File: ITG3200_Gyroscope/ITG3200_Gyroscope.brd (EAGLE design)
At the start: 39.7 x 26.7 mm, 5 parts

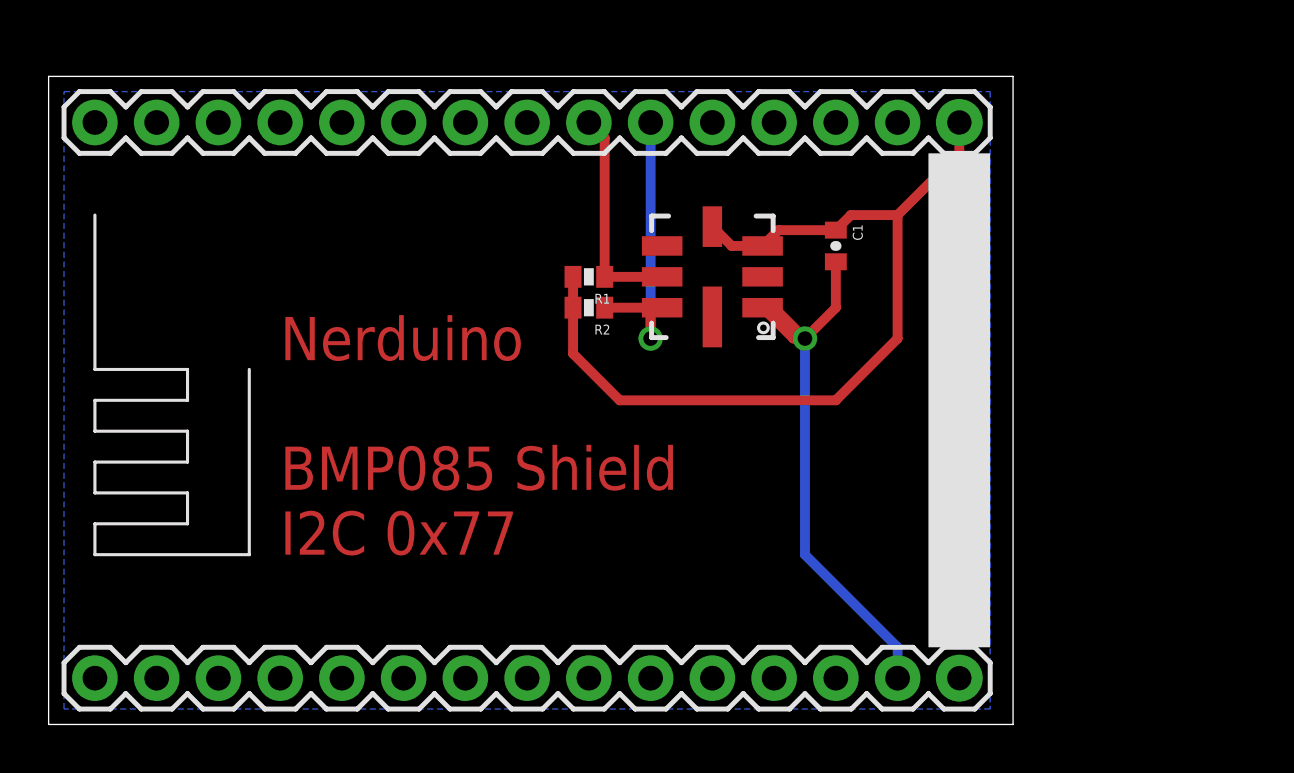
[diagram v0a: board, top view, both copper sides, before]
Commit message: Updated stencil text Added PCA9685 and ITG3200 shields
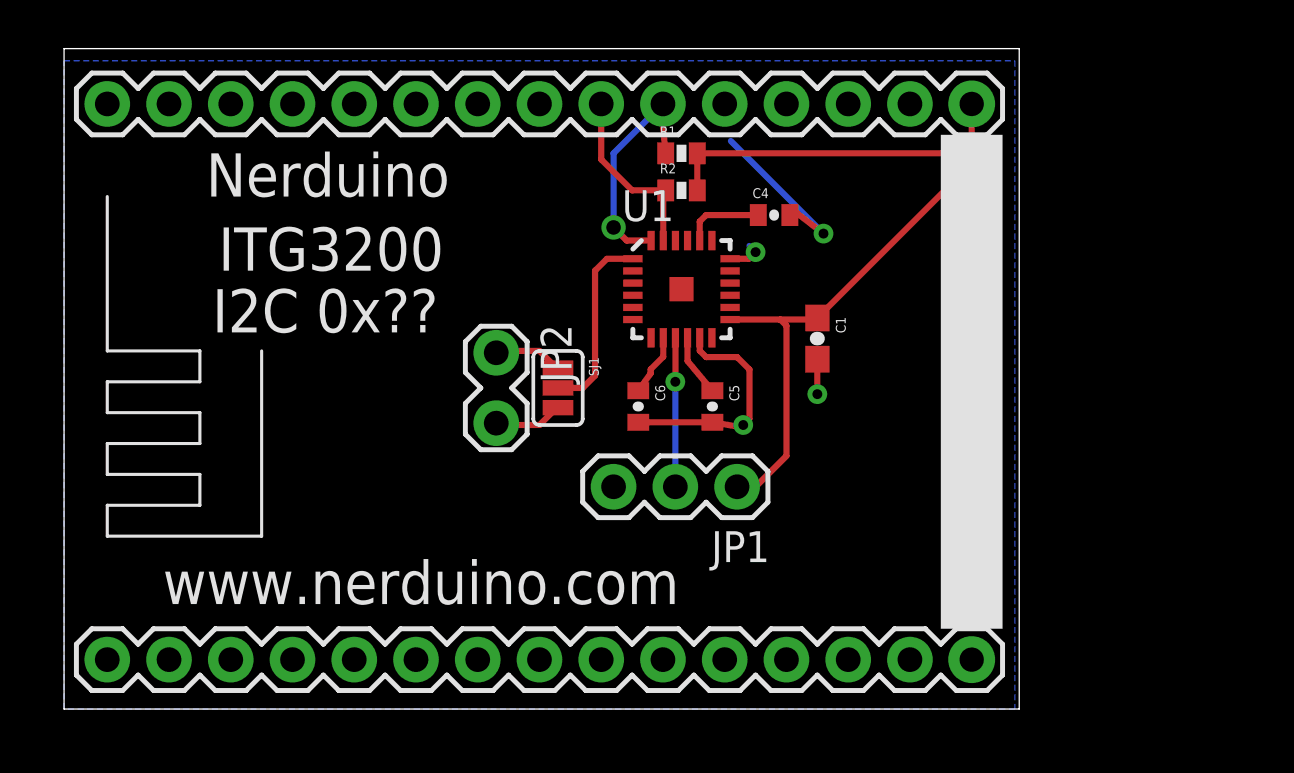
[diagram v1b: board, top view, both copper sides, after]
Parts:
- removed U$1: NERDSHIELD, NerduinoShieldLib:NERDUINO_STACK
- added C4: 2.2nF, SparkFun:0402-CAP
- added C5: .1uF, SparkFun:0402-CAP
- added C6: 10nF, SparkFun:0402-CAP
- added JP1: JP1, SparkFun:1X03
- added JP2: (no value), SparkFun:1X02_LOCK
- added SJ1: ClockSource, SparkFun:SJ_3_PASTE2&3
- added U1: ITG-3200, SparkFun:QFN-24
- C1: value 0.1uF -> .1uF; device SparkFun:0402-CAP -> SparkFun:0603-CAP
- R1, R2: value 4.7k -> 4.7K
- U$2: value BMP085 -> NERDSHIELD; device SparkFun:BMP085 -> NerduinoShieldLib:NERDUINO_STACK
- moved U$2 12.8 mm to (19.6, 7.11), turned to 0 degrees
- moved R1 6.35 mm to (25.4, 22.9), turned to 0 degrees
- moved R2 6.15 mm to (25.4, 21.3), turned to 0 degrees
- moved C1 3.89 mm to (31.0, 15.2)
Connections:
- removed net 3.3V: C1.1, R1.2, R2.2, U$1.16, U$2.3, U$2.4
- removed net N$3: R1.1, U$1.22, U$2.6
- new net +3V3: C1.1, JP1.1, R1.2, R2.2, U$2.16, U1.13
- new net N$1: JP1.2, U1.9
- new net N$10: JP2.1, SJ1.1
- new net N$11: SJ1.2, U1.1
- new net N$5: R2.1, U$2.22, U1.23
- new net N$6: C4.1, U1.20
- new net N$7: C5.1, U1.10
- new net N$8: C6.1, U1.8
- net GND: now also C4.2, C5.2, C6.2, JP1.3, JP2.2, SJ1.3, U$2.10, U$2.14, U$2.17, U$2.24, U1.11, U1.18; no longer U$1.14, U$2.1
- net N$2: now also R1.1, U$2.21, U1.24; no longer R2.1, U$1.21, U$2.7
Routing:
- net 3.3V: track 36.8 -> 0.00 mm
- net +3V3: track 0.00 -> 36.4 mm
- net N$3: track 8.98 -> 0.00 mm
- net N$11: track 0.00 -> 7.81 mm
- net N$5: track 0.00 -> 7.57 mm
- net N$1: track 0.00 -> 6.13 mm, vias 0 -> 1
- net N$6: track 0.00 -> 3.30 mm
- net N$10: track 0.00 -> 2.87 mm
- net N$2: track 12.5 -> 9.77 mm
- net N$8: track 0.00 -> 2.55 mm
- net N$7: track 0.00 -> 2.55 mm
- net GND: track 23.8 -> 23.1 mm, vias 1 -> 4
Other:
- board size 39.7 x 26.7 mm -> 39.3 x 27.2 mm
- board text added: "I2C 0x??"
- board text added: "ITG3200"
- board text added: "Nerduino"
- board text added: "www.nerduino.com"
- board text removed: "Nerduino BMP085 Shield I2C 0x77"

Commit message: Added OLED Shield Added LiPo Battery Charger Shield Updated outlines of all shields to match the cutout of the nodemcu board
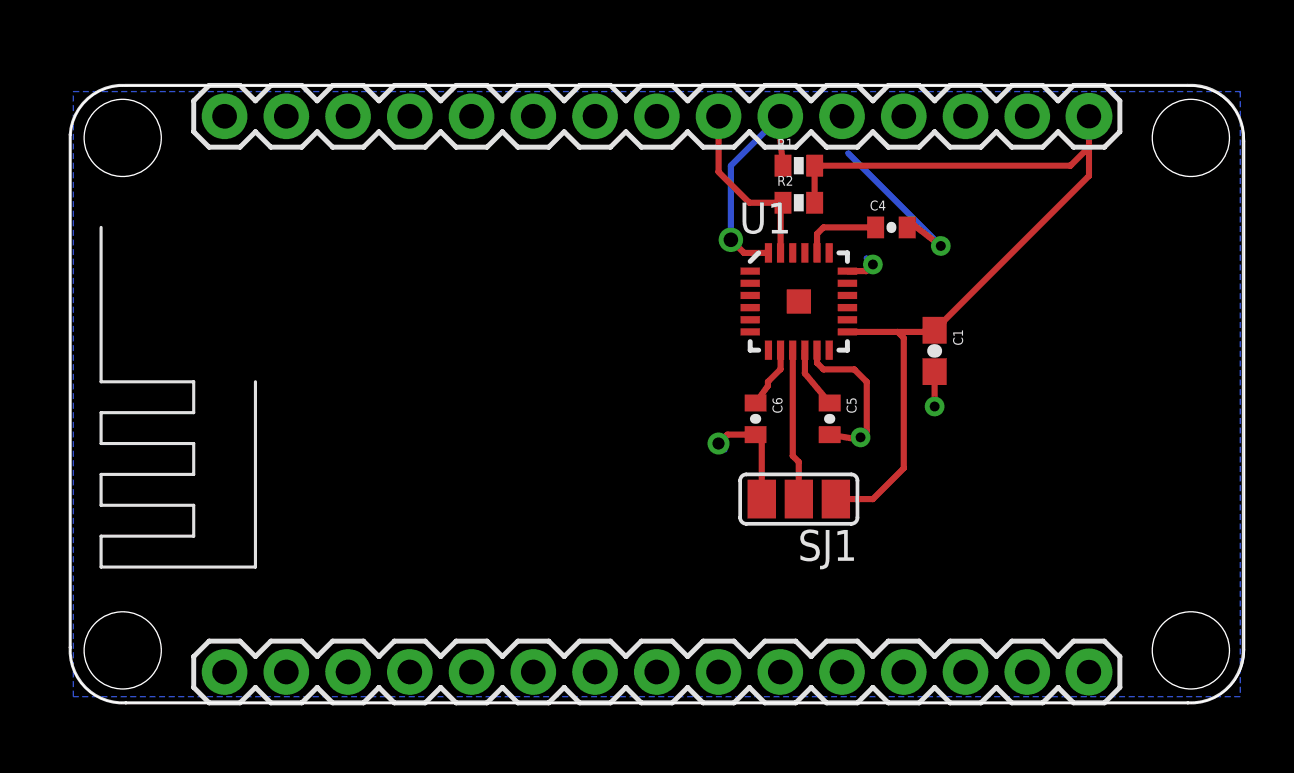
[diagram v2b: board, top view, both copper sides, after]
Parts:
- removed JP1: JP1, SparkFun:1X03
- removed JP2: (no value), SparkFun:1X02_LOCK
- SJ1: value ClockSource -> (none); device SparkFun:SJ_3_PASTE2&3 -> SparkFun:SJ_2
- moved SJ1 10.9 mm to (30.2, 8.64), turned to 180 degrees
- moved C1 4.85 mm to (35.8, 14.7)
- moved C4 4.85 mm to (34.0, 19.8)
- moved C6 4.85 mm to (28.4, 11.9)
- moved R1 4.85 mm to (30.2, 22.4)
- moved R2 4.85 mm to (30.2, 20.8)
- moved U$2 4.85 mm to (24.4, 6.60)
- moved U1 4.85 mm to (30.2, 16.8)
- moved C5 4.85 mm to (31.5, 11.9)
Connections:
- removed net N$10: JP2.1, SJ1.1
- removed net N$11: SJ1.2, U1.1
- net +3V3: now also SJ1.1; no longer JP1.1
- net GND: now also U1.1; no longer JP1.3, JP2.2
- net N$1: now also SJ1.2; no longer JP1.2
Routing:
- net N$11: track 7.81 -> 0.00 mm
- net N$10: track 2.87 -> 0.00 mm
- net GND: track 23.1 -> 21.9 mm, vias 4 -> 5
- net +3V3: track 36.4 -> 37.2 mm
- net N$1: track 6.13 -> 6.23 mm, vias 1 -> 0
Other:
- board size 39.3 x 27.2 mm -> 48.3 x 25.4 mm
- board text added: "NERDUINO ITG3200 Shield I2C 0x?? www.nerduino.com"
- board text removed: "I2C 0x??"
- board text removed: "ITG3200"
- board text removed: "Nerduino"
- board text removed: "www.nerduino.com"

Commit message: Updated the i2c pins to all shields to use d11/d12  as these pins will have dual use with the upcoming wifimcu Added FM24W256  Fram shield Added X95840 Digital potentiometer Shield Added AD5696 DAC Shield
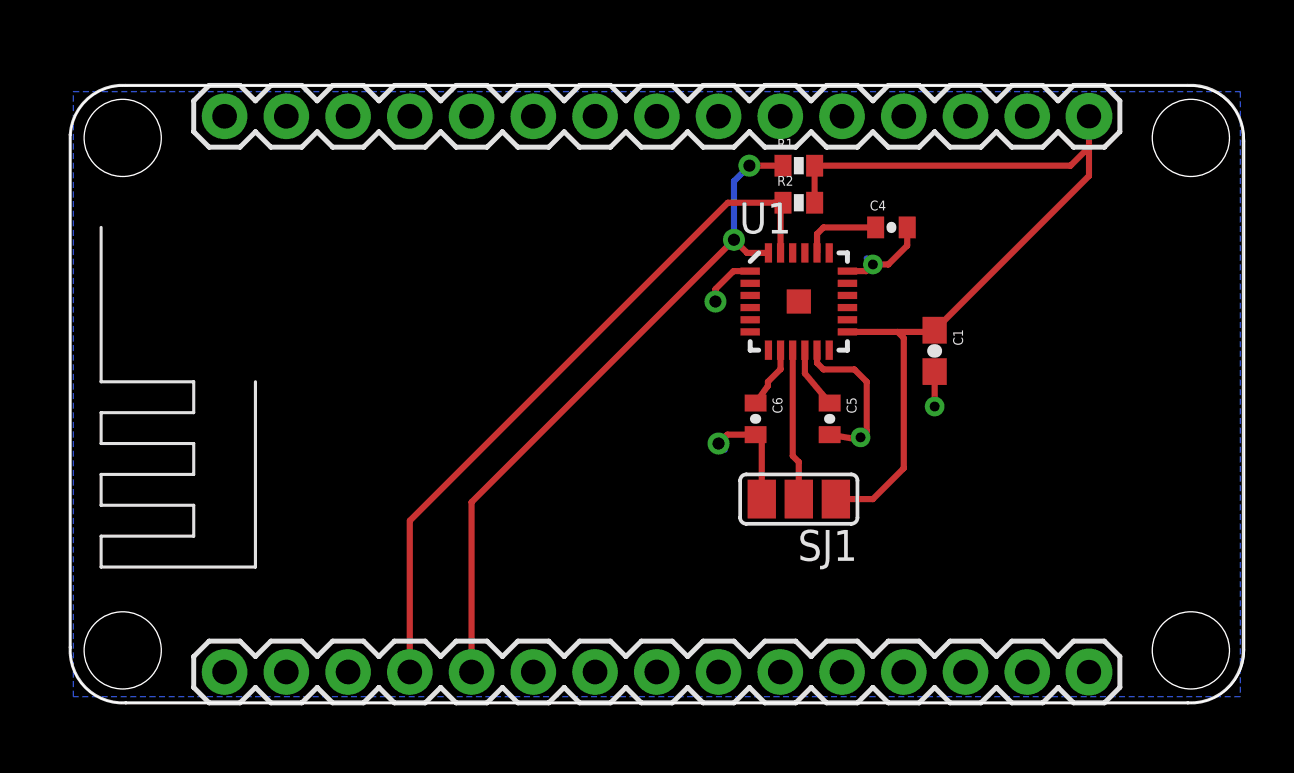
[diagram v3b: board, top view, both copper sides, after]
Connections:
- net GND: no longer U$2.24
- net N$2: now also U$2.5; no longer U$2.21
- net N$5: now also U$2.4; no longer U$2.22
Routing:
- net N$5: track 7.57 -> 29.1 mm
- net N$2: track 9.77 -> 28.6 mm, vias 1 -> 2
- net GND: track 21.9 -> 19.9 mm
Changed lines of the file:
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@@
 <contactref element="C5" pad="2"/>
 <contactref element="C4" pad="2"/>
-<wire x1="34.686" y1="19.812" x2="34.964" y2="19.9" width="0.254" layer="1"/>
-<wire x1="34.964" y1="19.9" x2="36.068" y2="19.05" width="0.254" layer="1"/>
-<wire x1="36.068" y1="19.05" x2="32.258" y2="22.86" width="0.254" layer="16"/>
 <wire x1="32.226" y1="18.014" x2="33" y2="18.014" width="0.254" layer="1"/>
 <wire x1="33" y1="18.014" x2="33.274" y2="18.288" width="0.254" layer="1"/>
@@
 <wire x1="35.814" y1="13.882" x2="35.814" y2="12.446" width="0.254" layer="1"/>
 <wire x1="35.814" y1="12.446" x2="36.068" y2="12.446" width="0.254" layer="16"/>
-<via x="36.068" y="19.05" extent="1-16" drill="0.4064" diameter="0.4064" shape="octagon"/>
 <via x="33.274" y="18.288" extent="1-16" drill="0.4064" diameter="0.4064" shape="octagon"/>
 <via x="32.766" y="11.176" extent="1-16" drill="0.4064" diameter="0.4064" shape="octagon"/>
@@
 </polygon>
 <contactref element="U$2" pad="17"/>
-<contactref element="U$2" pad="24"/>
 <contactref element="U$2" pad="14"/>
 <contactref element="U$2" pad="10"/>
@@
 <via x="26.924" y="10.922" extent="1-16" drill="0.5"/>
 <wire x1="26.924" y1="10.922" x2="27.178" y2="10.668" width="0.254" layer="16"/>
-<wire x1="32.226" y1="18.014" x2="28.226" y2="18.014" width="0" layer="19" extent="1-1"/>
+<wire x1="28.226" y1="18.014" x2="27.539" y2="18.014" width="0.254" layer="1"/>
+<wire x1="27.539" y1="18.014" x2="26.797" y2="17.272" width="0.254" layer="1"/>
+<wire x1="26.797" y1="17.272" x2="26.797" y2="16.764" width="0.254" layer="1"/>
+<via x="26.797" y="16.764" extent="1-16" drill="0.5"/>
+<wire x1="26.797" y1="16.764" x2="26.67" y2="16.764" width="0.254" layer="16"/>
+<wire x1="26.67" y1="16.764" x2="26.543" y2="16.891" width="0.254" layer="16"/>
+<wire x1="34.686" y1="19.812" x2="34.686" y2="19.065" width="0.254" layer="1"/>
+<wire x1="34.686" y1="19.065" x2="33.909" y2="18.288" width="0.254" layer="1"/>
+<wire x1="33.909" y1="18.288" x2="33.274" y2="18.288" width="0.254" layer="1"/>
 </signal>
 <signal name="N$2">
 <contactref element="R1" pad="1"/>
 <contactref element="U1" pad="24"/>
-<contactref element="U$2" pad="21"/>
-<wire x1="28.976" y1="18.764" x2="27.972" y2="18.764" width="0.254" layer="1"/>
-<wire x1="27.972" y1="18.764" x2="27.432" y2="19.304" width="0.254" layer="1"/>
-<via x="27.432" y="19.304" extent="1-16" drill="0.6" shape="square"/>
-<wire x1="27.432" y1="19.304" x2="27.432" y2="22.352" width="0.254" layer="16"/>
-<wire x1="27.432" y1="22.352" x2="29.464" y2="24.384" width="0.254" layer="16"/>
-<wire x1="29.576" y1="22.352" x2="29.376" y2="24.296" width="0.254" layer="1"/>
-<wire x1="29.376" y1="24.296" x2="29.464" y2="24.384" width="0.254" layer="1"/>
+<contactref element="U$2" pad="5"/>
+<wire x1="16.764" y1="1.524" x2="16.764" y2="8.509" width="0.254" layer="1"/>
+<wire x1="16.764" y1="8.509" x2="27.559" y2="19.304" width="0.254" layer="1"/>
+<via x="27.559" y="19.304" extent="1-16" drill="0.5"/>
+<wire x1="27.559" y1="19.304" x2="27.559" y2="21.717" width="0.254" layer="16"/>
+<wire x1="27.559" y1="21.717" x2="28.194" y2="22.352" width="0.254" layer="16"/>
+<via x="28.194" y="22.352" extent="1-16" drill="0.5"/>
+<wire x1="28.194" y1="22.352" x2="29.576" y2="22.352" width="0.254" layer="1"/>
+<wire x1="28.976" y1="18.764" x2="28.099" y2="18.764" width="0.254" layer="1"/>
+<wire x1="28.099" y1="18.764" x2="27.559" y2="19.304" width="0.254" layer="1"/>
 </signal>
 <signal name="N$5">
 <contactref element="R2" pad="1"/>
 <contactref element="U1" pad="23"/>
-<contactref element="U$2" pad="22"/>
-<wire x1="26.924" y1="24.384" x2="26.924" y2="22.098" width="0.254" layer="1"/>
-<wire x1="26.924" y1="22.098" x2="28.194" y2="20.828" width="0.254" layer="1"/>
-<wire x1="28.194" y1="20.828" x2="29.576" y2="20.828" width="0.254" layer="1"/>
-<wire x1="29.476" y1="18.764" x2="29.476" y2="20.728" width="0.254" layer="1"/>
+<wire x1="29.476" y1="18.764" x2="29.476" y2="20.574" width="0.254" layer="1"/>
+<wire x1="29.476" y1="20.574" x2="29.476" y2="20.728" width="0.254" layer="1"/>
 <wire x1="29.476" y1="20.728" x2="29.576" y2="20.828" width="0.254" layer="1"/>
+<contactref element="U$2" pad="4"/>
+<wire x1="14.224" y1="1.524" x2="14.224" y2="7.747" width="0.254" layer="1"/>
+<wire x1="14.224" y1="7.747" x2="27.305" y2="20.828" width="0.254" layer="1"/>
+<wire x1="27.305" y1="20.828" x2="29.222" y2="20.828" width="0.254" layer="1"/>
+<wire x1="29.222" y1="20.828" x2="29.476" y2="20.574" width="0.254" layer="1"/>
 </signal>
 <signal name="+3V3">
